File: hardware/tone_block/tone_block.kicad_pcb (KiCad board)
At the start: 2 copper layers, 48 x 20 mm, 41 parts, among them J1 conn_1x3, J2 conn_1x3, Q1 RS32716R, Q2 LBSS84LT1G, SW1 DPDT, U1 TLV170IDBVR

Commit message: Added ext cap option
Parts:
- added J3: conn_1x2, Connector_PinHeader_2.54mm:PinHeader_1x02_P2.54mm_Vertical, B.Cu at (223.8, 118.5)
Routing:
- net Net-(Freq1-PadC): track 41.2 -> 47.4 mm
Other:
- board text added: "EXT CAP"
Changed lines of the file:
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@@
     (tags "capacitor")
     (property "LCSC" "C307331")
-    (property "LCSC Part Number" "C307331")
     (property "Sheetfile" "tone_block.kicad_sch")
     (property "Sheetname" "")
@@
     (tags "capacitor")
     (property "LCSC" "C440198")
-    (property "LCSC Part Number" "C15850")
     (property "Sheetfile" "tone_block.kicad_sch")
     (property "Sheetname" "")
@@
     (tags "resistor")
     (property "LCSC" "C25741")
-    (property "LCSC Part Number" "C25741")
     (property "Sheetfile" "tone_block.kicad_sch")
     (property "Sheetname" "")
@@
     (tags "resistor")
     (property "LCSC" "C25104")
-    (property "LCSC Part Number" "C25104")
     (property "Sheetfile" "tone_block.kicad_sch")
     (property "Sheetname" "")
@@
     (tags "resistor")
     (property "LCSC" "C25104")
-    (property "LCSC Part Number" "C25104")
     (property "Sheetfile" "tone_block.kicad_sch")
     (property "Sheetname" "")
@@
     (tags "resistor")
     (property "LCSC" "C25104")
-    (property "LCSC Part Number" "C25104")
     (property "Sheetfile" "tone_block.kicad_sch")
     (property "Sheetname" "")
@@
     (tags "resistor")
     (property "LCSC" "C25104")
-    (property "LCSC Part Number" "C25104")
     (property "Sheetfile" "tone_block.kicad_sch")
     (property "Sheetname" "")
@@
     (tags "resistor")
     (property "LCSC" "C25741")
-    (property "LCSC Part Number" "C25741")
     (property "Sheetfile" "tone_block.kicad_sch")
     (property "Sheetname" "")
@@
     (tags "capacitor")
     (property "LCSC" "C1779")
-    (property "LCSC Part Number" "C1779")
     (property "Sheetfile" "tone_block.kicad_sch")
     (property "Sheetname" "")
@@
     (tags "resistor")
     (property "LCSC" "C25104")
-    (property "LCSC Part Number" "C25104")
     (property "Sheetfile" "tone_block.kicad_sch")
     (property "Sheetname" "")
@@
     (tags "resistor")
     (property "LCSC" "C25104")
-    (property "LCSC Part Number" "C25104")
     (property "Sheetfile" "tone_block.kicad_sch")
     (property "Sheetname" "")
@@
     (tags "resistor")
     (property "LCSC" "C25104")
-    (property "LCSC Part Number" "C25104")
     (property "Sheetfile" "tone_block.kicad_sch")
     (property "Sheetname" "")
@@
     (tags "capacitor")
     (property "LCSC" "C1622")
-    (property "LCSC Part Number" "C1622")
     (property "Sheetfile" "tone_block.kicad_sch")
     (property "Sheetname" "")
@@
     (tags "resistor")
     (property "LCSC" "C25104")
-    (property "LCSC Part Number" "C25104")
     (property "Sheetfile" "tone_block.kicad_sch")
     (property "Sheetname" "")
@@
     )
   )
+  (footprint "Connector_PinHeader_2.54mm:PinHeader_1x02_P2.54mm_Vertical" (layer "B.Cu")
+    (at 223.75 118.5 -90)
+    (descr "Through hole straight pin header, 1x02, 2.54mm pitch, single row")
+    (tags "Through hole pin header THT 1x02 2.54mm single row")
+    (property "Sheetfile" "tone_block.kicad_sch")
+    (property "Sheetname" "")
+    (attr through_hole)
+    (fp_text reference "J3" (at 0 3.6 90) (layer "B.SilkS") hide
+      (effects (font (size 1 1) (thickness 0.15)) (justify mirror))
+    )
+    (fp_text value "conn_1x2" (at 0 -3.6 90) (layer "B.Fab")
+      (effects (font (size 1 1) (thickness 0.15)) (justify mirror))
+    )
+    (fp_text user "${REFERENCE}" (at 0 0 180) (layer "B.Fab")
+      (effects (font (size 1 1) (thickness 0.15)) (justify mirror))
+    )
+    (fp_line (start 1.33 0) (end 1.33 -2.6) (layer "B.SilkS") (width 0.12))
+    (fp_line (start -1.33 1.27) (end -1.33 2.6) (layer "B.SilkS") (width 0.12))
+    (fp_line (start -1.33 2.6) (end 0 2.6) (layer "B.SilkS") (width 0.12))
+    (fp_line (start -1.33 0) (end -1.33 -2.6) (layer "B.SilkS") (width 0.12))
+    (fp_line (start -1.33 -2.6) (end 1.33 -2.6) (layer "B.SilkS") (width 0.12))
+    (fp_line (start -1.33 0) (end 1.33 0) (layer "B.SilkS") (width 0.12))
+    (fp_line (start 1.8 3.07) (end -1.8 3.07) (layer "B.CrtYd") (width 0.05))
+    (fp_line (start -1.8 -3.08) (end 1.8 -3.08) (layer "B.CrtYd") (width 0.05))
+    (fp_line (start 1.8 -3.08) (end 1.8 3.07) (layer "B.CrtYd") (width 0.05))
+    (fp_line (start -1.8 3.07) (end -1.8 -3.08) (layer "B.CrtYd") (width 0.05))
+    (fp_line (start -0.635 2.54) (end 1.27 2.54) (layer "B.Fab") (width 0.1))
+    (fp_line (start -1.27 -2.54) (end -1.27 1.905) (layer "B.Fab") (width 0.1))
+    (fp_line (start 1.27 -2.54) (end -1.27 -2.54) (layer "B.Fab") (width 0.1))
+    (fp_line (start -1.27 1.905) (end -0.635 2.54) (layer "B.Fab") (width 0.1))
+    (fp_line (start 1.27 2.54) (end 1.27 -2.54) (layer "B.Fab") (width 0.1))
+    (pad "1" thru_hole rect (at 0 1.27 270) (size 1.7 1.7) (drill 1) (layers *.Cu *.Mask)
+      (net 27 "Net-(Freq1-PadC)") (pinfunction "P1") (pintype "passive"))
+    (pad "2" thru_hole oval (at 0 -1.27 270) (size 1.7 1.7) (drill 1) (layers *.Cu *.Mask)
+      (net 1 "GND") (pinfunction "P2") (pintype "passive"))
+    (model "${KICAD6_3DMODEL_DIR}/Connector_PinHeader_2.54mm.3dshapes/PinHeader_1x02_P2.54mm_Vertical.wrl" hide
+      (offset (xyz 0 1.27 0))
+      (scale (xyz 1 1 1))
+      (rotate (xyz 0 0 0))
+    )
+  )
   (footprint "Resistor_SMD:R_0402_1005Metric" (layer "B.Cu")
     (at 209 109 -90)
@@
     (tags "resistor")
     (property "LCSC" "C25900")
-    (property "LCSC Part Number" "C25900")
     (property "Sheetfile" "tone_block.kicad_sch")
     (property "Sheetname" "")
@@
     (tags "SOT TO_SOT_SMD")
     (property "LCSC" "C8492")
-    (property "LCSC Part Number" "C8492")
     (property "Sheetfile" "tone_block.kicad_sch")
     (property "Sheetname" "")
@@
     (tags "capacitor")
     (property "LCSC" "C440198")
-    (property "LCSC Part Number" "C15850")
     (property "Sheetfile" "tone_block.kicad_sch")
     (property "Sheetname" "")
@@
     (tags "capacitor")
     (property "LCSC" "C1622")
-    (property "LCSC Part Number" "C1622")
     (property "Sheetfile" "tone_block.kicad_sch")
     (property "Sheetname" "")
@@
     (tags "capacitor")
     (property "LCSC" "C1622")
-    (property "LCSC Part Number" "C1622")
     (property "Sheetfile" "tone_block.kicad_sch")
     (property "Sheetname" "")
@@
     (tags "capacitor")
     (property "LCSC" "C1622")
-    (property "LCSC Part Number" "C1622")
     (property "Sheetfile" "tone_block.kicad_sch")
     (property "Sheetname" "")
@@
     (tags "resistor")
     (property "LCSC" "C25104")
-    (property "LCSC Part Number" "C25104")
     (property "Sheetfile" "tone_block.kicad_sch")
     (property "Sheetname" "")
@@
     (tags "resistor")
     (property "LCSC" "C25104")
-    (property "LCSC Part Number" "C25104")
     (property "Sheetfile" "tone_block.kicad_sch")
     (property "Sheetname" "")
@@
     (tags "capacitor")
     (property "LCSC" "C1622")
-    (property "LCSC Part Number" "C1622")
     (property "Sheetfile" "tone_block.kicad_sch")
     (property "Sheetname" "")
@@
     (tags "resistor")
     (property "LCSC" "C25104")
-    (property "LCSC Part Number" "C25104")
     (property "Sheetfile" "tone_block.kicad_sch")
     (property "Sheetname" "")
@@
     (tags "capacitor")
     (property "LCSC" "C1622")
-    (property "LCSC Part Number" "C1622")
     (property "Sheetfile" "tone_block.kicad_sch")
     (property "Sheetname" "")
@@
     (tags "capacitor")
     (property "LCSC" "C1622")
-    (property "LCSC Part Number" "C1622")
     (property "Sheetfile" "tone_block.kicad_sch")
     (property "Sheetname" "")
@@
     (tags "capacitor")
     (property "LCSC" "C1622")
-    (property "LCSC Part Number" "C1622")
     (property "Sheetfile" "tone_block.kicad_sch")
     (property "Sheetname" "")
@@
     (tags "capacitor")
     (property "LCSC" "C1622")
-    (property "LCSC Part Number" "C1622")
     (property "Sheetfile" "tone_block.kicad_sch")
     (property "Sheetname" "")
@@
     (tags "resistor")
     (property "LCSC" "C25104")
-    (property "LCSC Part Number" "C25104")
     (property "Sheetfile" "tone_block.kicad_sch")
     (property "Sheetname" "")
@@
     (tags "resistor")
     (property "LCSC" "C25104")
-    (property "LCSC Part Number" "C25104")
     (property "Sheetfile" "tone_block.kicad_sch")
     (property "Sheetname" "")
@@
   )
   (gr_text "V+" (at 212.5 116) (layer "B.SilkS")
+    (effects (font (size 0.8 0.8) (thickness 0.15)) (justify mirror))
+  )
+  (gr_text "EXT CAP" (at 223.75 116) (layer "B.SilkS")
     (effects (font (size 0.8 0.8) (thickness 0.15)) (justify mirror))
   )
@@
   (segment (start 216.88 113) (end 216.88 111.91) (width 0.25) (layer "B.Cu") (net 27))
   (segment (start 215.91 114.7) (end 215.91 113.6) (width 0.25) (layer "B.Cu") (net 27))
+  (segment (start 222.39 118.5) (end 222.48 118.5) (width 0.25) (layer "B.Cu") (net 27))
   (segment (start 204.52548 108.02548) (end 204.25 107.75) (width 0.25) (layer "B.Cu") (net 27))
   (segment (start 216.88 111.91) (end 216.89 111.9) (width 0.25) (layer "B.Cu") (net 27))
@@
   (segment (start 216.28 113.6) (end 216.88 113) (width 0.25) (layer "B.Cu") (net 27))
   (segment (start 216.89 109.52) (end 217.91 108.5) (width 0.25) (layer "B.Cu") (net 27))
+  (segment (start 218.09 114.2) (end 222.39 118.5) (width 0.25) (layer "B.Cu") (net 27))
   (zone (net 1) (net_name "GND") (layer "F.Cu") (hatch edge 0.508)
     (connect_pads (clearance 0.508))

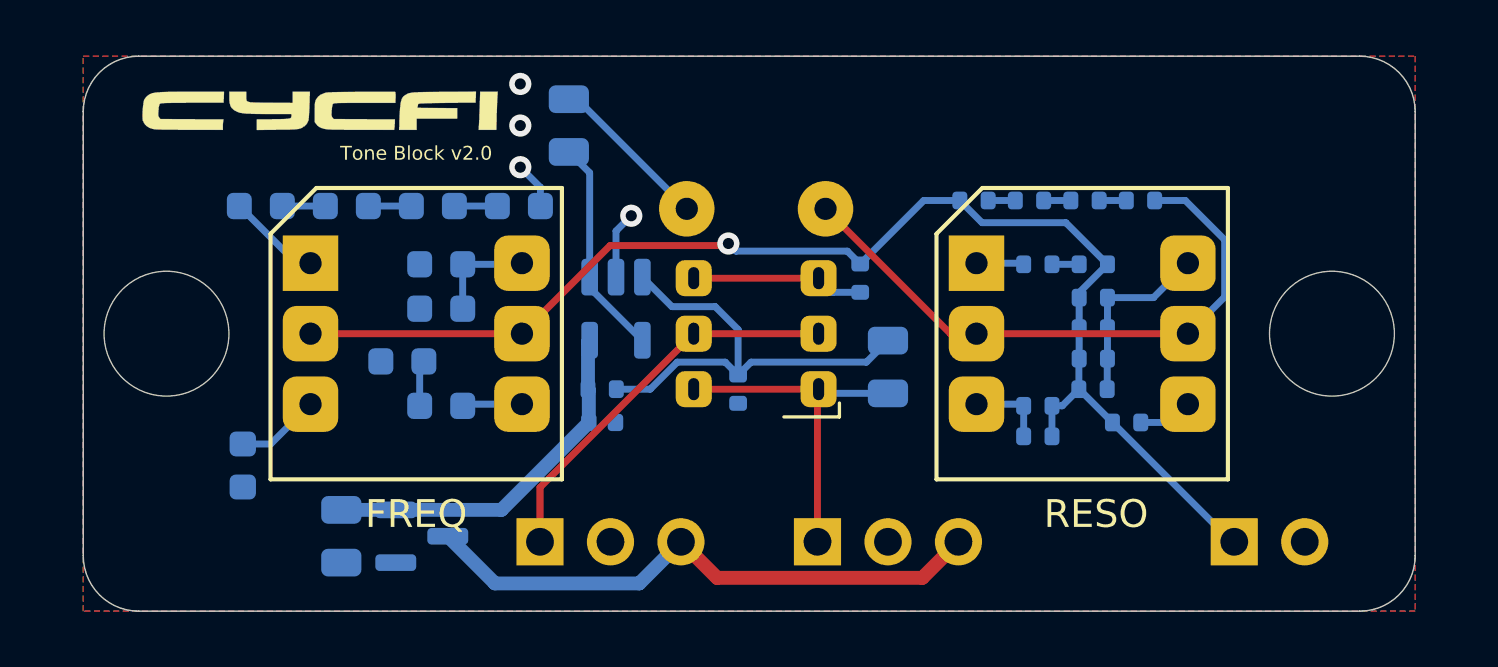
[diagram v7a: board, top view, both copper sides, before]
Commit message: Added bleed resistors
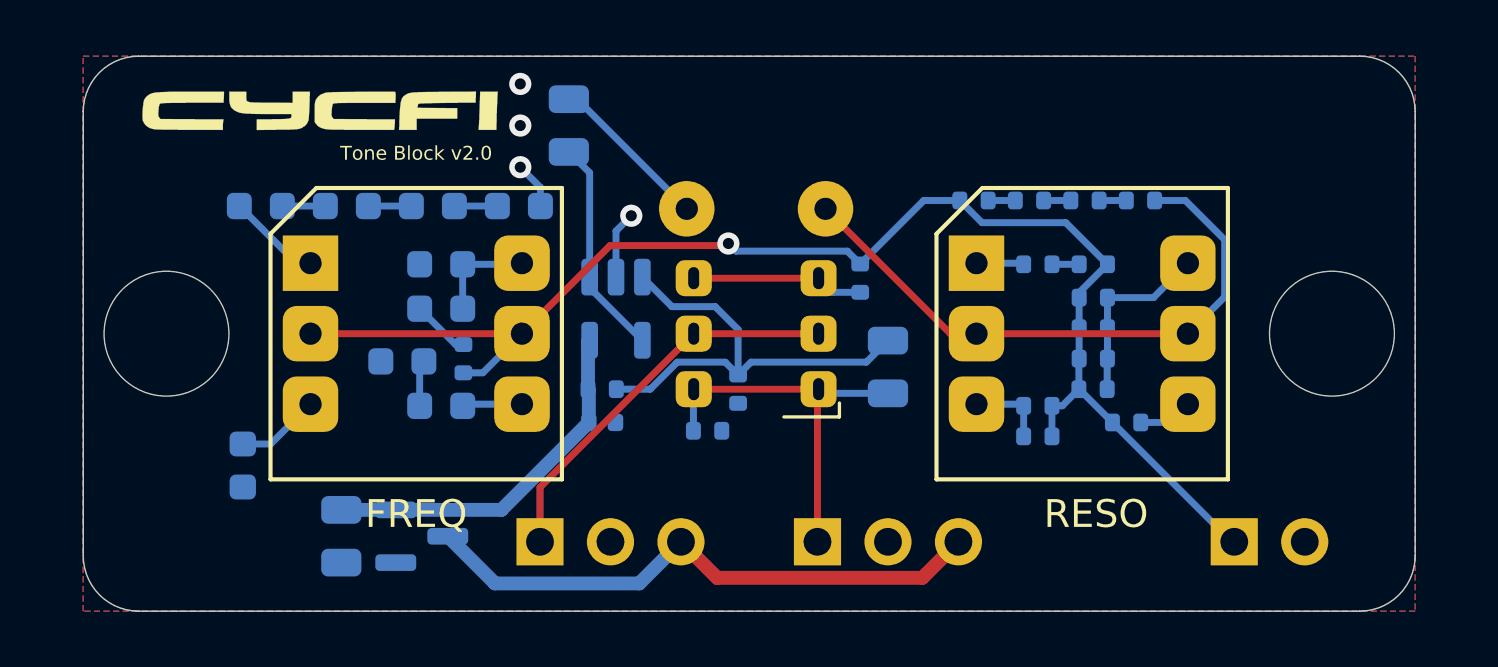
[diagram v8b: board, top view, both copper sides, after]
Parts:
- added R17: 47k, Resistor_SMD:R_0402_1005Metric, B.Cu at (203.5, 114.5)
- added R18: 47k, Resistor_SMD:R_0402_1005Metric, B.Cu at (194.7, 111.9)
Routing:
- net Net-(Freq1-PadC): track 47.4 -> 50.1 mm
- net GND: track 4.14 -> 6.25 mm
- net in: track 12.6 -> 14.1 mm
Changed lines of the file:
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@@
+    )
+  )
+  (footprint "Resistor_SMD:R_0402_1005Metric" (layer "B.Cu")
+    (at 194.7 111.9 -90)
+    (descr "Resistor SMD 0402 (1005 Metric), square (rectangular) end terminal, IPC_7351 nominal, (Body size source: IPC-SM-782 page 72, https://www.pcb-3d.com/wordpress/wp-content/uploads/ipc-sm-782a_amendment_1_and_2.pdf), generated with kicad-footprint-generator")
+    (tags "resistor")
+    (property "LCSC" "C25900")
+    (property "Sheetfile" "tone_block.kicad_sch")
+    (property "Sheetname" "")
+    (attr smd)
+    (fp_text reference "R18" (at 0 1.17 90) (layer "B.SilkS") hide
+      (effects (font (size 1 1) (thickness 0.15)) (justify mirror))
+    )
+    (fp_text value "47k" (at 0 -1.17 90) (layer "B.Fab")
+      (effects (font (size 1 1) (thickness 0.15)) (justify mirror))
+    )
+    (fp_text user "${REFERENCE}" (at 0 0 90) (layer "B.Fab")
+      (effects (font (size 0.26 0.26) (thickness 0.04)) (justify mirror))
+    )
+    (fp_line (start -0.153641 0.38) (end 0.153641 0.38) (layer "B.SilkS") (width 0.12))
+    (fp_line (start -0.153641 -0.38) (end 0.153641 -0.38) (layer "B.SilkS") (width 0.12))
+    (fp_line (start -0.93 0.47) (end 0.93 0.47) (layer "B.CrtYd") (width 0.05))
+    (fp_line (start -0.93 -0.47) (end -0.93 0.47) (layer "B.CrtYd") (width 0.05))
+    (fp_line (start 0.93 0.47) (end 0.93 -0.47) (layer "B.CrtYd") (width 0.05))
+    (fp_line (start 0.93 -0.47) (end -0.93 -0.47) (layer "B.CrtYd") (width 0.05))
+    (fp_line (start -0.525 0.27) (end 0.525 0.27) (layer "B.Fab") (width 0.1))
+    (fp_line (start -0.525 -0.27) (end -0.525 0.27) (layer "B.Fab") (width 0.1))
+    (fp_line (start 0.525 -0.27) (end -0.525 -0.27) (layer "B.Fab") (width 0.1))
+    (fp_line (start 0.525 0.27) (end 0.525 -0.27) (layer "B.Fab") (width 0.1))
+    (pad "1" smd roundrect (at -0.51 0 270) (size 0.54 0.64) (layers "B.Cu" "B.Paste" "B.Mask") (roundrect_rratio 0.25)
+      (net 1 "GND") (pintype "passive"))
+    (pad "2" smd roundrect (at 0.51 0 270) (size 0.54 0.64) (layers "B.Cu" "B.Paste" "B.Mask") (roundrect_rratio 0.25)
+      (net 27 "Net-(Freq1-PadC)") (pintype "passive"))
+    (model "${KICAD6_3DMODEL_DIR}/Resistor_SMD.3dshapes/R_0402_1005Metric.wrl"
+      (offset (xyz 0 0 0))
+      (scale (xyz 1 1 1))
+      (rotate (xyz 0 0 0))
     )
   )
@@
   )
   (footprint "Resistor_SMD:R_0402_1005Metric" (layer "B.Cu")
+    (at 203.5 114.5 180)
+    (descr "Resistor SMD 0402 (1005 Metric), square (rectangular) end terminal, IPC_7351 nominal, (Body size source: IPC-SM-782 page 72, https://www.pcb-3d.com/wordpress/wp-content/uploads/ipc-sm-782a_amendment_1_and_2.pdf), generated with kicad-footprint-generator")
+    (tags "resistor")
+    (property "LCSC" "C25900")
+    (property "Sheetfile" "tone_block.kicad_sch")
+    (property "Sheetname" "")
+    (attr smd)
+    (fp_text reference "R17" (at 0 1.17) (layer "B.SilkS") hide
+      (effects (font (size 1 1) (thickness 0.15)) (justify mirror))
+    )
+    (fp_text value "47k" (at 0 -1.17) (layer "B.Fab")
+      (effects (font (size 1 1) (thickness 0.15)) (justify mirror))
+    )
+    (fp_text user "${REFERENCE}" (at 0 0) (layer "B.Fab")
+      (effects (font (size 0.26 0.26) (thickness 0.04)) (justify mirror))
+    )
+    (fp_line (start -0.153641 -0.38) (end 0.153641 -0.38) (layer "B.SilkS") (width 0.12))
+    (fp_line (start -0.153641 0.38) (end 0.153641 0.38) (layer "B.SilkS") (width 0.12))
+    (fp_line (start -0.93 -0.47) (end -0.93 0.47) (layer "B.CrtYd") (width 0.05))
+    (fp_line (start 0.93 -0.47) (end -0.93 -0.47) (layer "B.CrtYd") (width 0.05))
+    (fp_line (start -0.93 0.47) (end 0.93 0.47) (layer "B.CrtYd") (width 0.05))
+    (fp_line (start 0.93 0.47) (end 0.93 -0.47) (layer "B.CrtYd") (width 0.05))
+    (fp_line (start 0.525 -0.27) (end -0.525 -0.27) (layer "B.Fab") (width 0.1))
+    (fp_line (start -0.525 -0.27) (end -0.525 0.27) (layer "B.Fab") (width 0.1))
+    (fp_line (start 0.525 0.27) (end 0.525 -0.27) (layer "B.Fab") (width 0.1))
+    (fp_line (start -0.525 0.27) (end 0.525 0.27) (layer "B.Fab") (width 0.1))
+    (pad "1" smd roundrect (at -0.51 0 180) (size 0.54 0.64) (layers "B.Cu" "B.Paste" "B.Mask") (roundrect_rratio 0.25)
+      (net 1 "GND") (pintype "passive"))
+    (pad "2" smd roundrect (at 0.51 0 180) (size 0.54 0.64) (layers "B.Cu" "B.Paste" "B.Mask") (roundrect_rratio 0.25)
+      (net 3 "in") (pintype "passive"))
+    (model "${KICAD6_3DMODEL_DIR}/Resistor_SMD.3dshapes/R_0402_1005Metric.wrl"
+      (offset (xyz 0 0 0))
+      (scale (xyz 1 1 1))
+      (rotate (xyz 0 0 0))
+    )
+  )
+  (footprint "Resistor_SMD:R_0402_1005Metric" (layer "B.Cu")
     (at 217.39 113)
     (descr "Resistor SMD 0402 (1005 Metric), square (rectangular) end terminal, IPC_7351 nominal, (Body size source: IPC-SM-782 page 72, https://www.pcb-3d.com/wordpress/wp-content/uploads/ipc-sm-782a_amendment_1_and_2.pdf), generated with kicad-footprint-generator")
@@
   (segment (start 197.475 106.4) (end 197.475 105.725) (width 0.25) (layer "B.Cu") (net 1))
   (segment (start 197.475 105.725) (end 196.75 105) (width 0.25) (layer "B.Cu") (net 1))
+  (segment (start 194.415 111.39) (end 193.125 110.1) (width 0.25) (layer "B.Cu") (net 1))
+  (segment (start 194.7 111.39) (end 194.415 111.39) (width 0.25) (layer "B.Cu") (net 1))
   (segment (start 198.8 102.55) (end 202.75 106.5) (width 0.25) (layer "B.Cu") (net 2))
   (segment (start 198.5 102.55) (end 198.8 102.55) (width 0.25) (layer "B.Cu") (net 2))
@@
   (segment (start 207.5 113) (end 203 113) (width 0.25) (layer "F.Cu") (net 3))
   (segment (start 210 113.15) (end 207.65 113.15) (width 0.25) (layer "B.Cu") (net 3))
+  (segment (start 202.99 113.01) (end 203 113) (width 0.25) (layer "B.Cu") (net 3))
+  (segment (start 202.99 114.5) (end 202.99 113.01) (width 0.25) (layer "B.Cu") (net 3))
   (segment (start 207.65 113.15) (end 207.5 113) (width 0.25) (layer "B.Cu") (net 3))
   (segment (start 190.3 117.35) (end 192.2625 117.35) (width 0.5) (layer "B.Cu") (net 4))
@@
   (segment (start 213.39 107) (end 212.59 106.2) (width 0.25) (layer "B.Cu") (net 27))
   (segment (start 208.53548 108.02548) (end 204.52548 108.02548) (width 0.25) (layer "B.Cu") (net 27))
+  (segment (start 194.7 112.41) (end 195.4 112.41) (width 0.25) (layer "B.Cu") (net 27))
   (segment (start 216.89 111.9) (end 216.89 110.8) (width 0.25) (layer "B.Cu") (net 27))
   (segment (start 216.88 113) (end 216.88 111.91) (width 0.25) (layer "B.Cu") (net 27))
@@
   (segment (start 204.52548 108.02548) (end 204.25 107.75) (width 0.25) (layer "B.Cu") (net 27))
   (segment (start 216.88 111.91) (end 216.89 111.9) (width 0.25) (layer "B.Cu") (net 27))
+  (segment (start 195.4 112.41) (end 196.81 111) (width 0.25) (layer "B.Cu") (net 27))
   (segment (start 212.59 106.2) (end 211.29 106.2) (width 0.25) (layer "B.Cu") (net 27))
   (segment (start 216.89 113) (end 218.09 114.2) (width 0.25) (layer "B.Cu") (net 27))
